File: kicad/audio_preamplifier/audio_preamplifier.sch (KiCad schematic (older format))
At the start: 33 parts, among them P1 CONN_01X05, P2 CONN_01X03, P3 CONN_01X03, P4 CONN_01X02, U1 PIC12F629, U2 78L05, U3 TL072

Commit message: new kicad version components in schematics
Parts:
- removed C10, C2, C3: 100n, symbol C
- removed P1: CONN_01X05, symbol CONN_01X05
- removed R1: 10k, symbol R
- removed R5, R6, R7: 3k3, symbol R
- removed U1: PIC12F629, SOIC, symbol PIC12F629
- removed U2: 78L05, symbol 78L05
- C1: value 100m -> 100m/25V; footprint (none) -> Capacitors_SMD:c_elec_6.3x7.7; symbol C -> CP
- C11: footprint (none) -> Capacitors_SMD:C_1206_HandSoldering
- C4: value 47m -> 47m/25V; footprint (none) -> Capacitors_Tantalum_SMD:TantalC_SizeD_EIA-7343_HandSoldering; symbol C -> CP
- C5: value 2m2 -> 2m2/16V; footprint (none) -> Capacitors_Tantalum_SMD:TantalC_SizeA_EIA-3216_HandSoldering; symbol C -> CP
- C6, C7: value 10m -> 10m/16V; footprint (none) -> Capacitors_SMD:c_elec_5x5.8; symbol C -> CP
- C8, C9: value 47m -> 47m/25V; footprint (none) -> Capacitors_SMD:c_elec_5x5.8; symbol C -> CP
- P2, P3: footprint (none) -> Pin_Headers:Pin_Header_Straight_1x03
- P4: footprint (none) -> Pin_Headers:Pin_Header_Straight_1x02
- R10, R11, R12, R13, R14, R15, R16, R17, R8, R9: footprint (none) -> Resistors_SMD:R_1206_HandSoldering
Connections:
- net labels added: 12V_filtered, virtual_gnd
- net labels removed: +5V, CLK, DataIn, DataOut, GND, POWER_CTL
- wire segments 84 -> 62
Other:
- moved on the sheet: C11, L1, P2, P3, P4, R10, R11, R12, R13, R14, R15, R16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

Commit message: update parts for new version of kicad
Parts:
- U3: symbol TL072 -> TL072-RESCUE-audio_preamplifier
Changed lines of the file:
@@
 EESchema Schematic File Version 2
+LIBS:audio_preamplifier-rescue
 LIBS:power
 LIBS:device
@@
 LIBS:contrib
 LIBS:valves
-LIBS:audio_preamplifier-rescue
 LIBS:audio_preamplifier-cache
 EELAYER 25 0
@@
 $EndComp
 $Comp
-L TL072 U3
+L TL072-RESCUE-audio_preamplifier U3
 U 2 1 52D3B907
 P 3850 3800
@@
 $EndComp
 $Comp
-L TL072 U3
+L TL072-RESCUE-audio_preamplifier U3
 U 1 1 52D3B8FE
 P 3900 1850

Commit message: fix values
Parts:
- removed P4: CONN_01X02, Pin_Headers:Pin_Header_Straight_1x02, symbol CONN_01X02
- P3: footprint Pin_Headers:Pin_Header_Straight_1x03 -> Pin_Headers:Pin_Header_Straight_1x05; symbol CONN_01X03 -> CONN_01X05
- R14, R15: value 330k -> 100k
- R16, R17: value 7M5 -> 2M2
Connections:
- net +12V: now also P3.5 (P5)
- net AGND: now also P3.4 (P4)
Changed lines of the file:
@@
 L AGND #PWR03
 U 1 1 52EA31C6
-P 7950 4900
-F 0 "#PWR03" H 7950 4900 40  0001 C CNN
-F 1 "AGND" H 7950 4830 50  0000 C CNN
-F 2 "" H 7950 4900 60  0001 C CNN
-F 3 "" H 7950 4900 60  0001 C CNN
-	1    7950 4900
+P 8100 4000
+F 0 "#PWR03" H 8100 4000 40  0001 C CNN
+F 1 "AGND" H 8100 3930 50  0000 C CNN
+F 2 "" H 8100 4000 60  0001 C CNN
+F 3 "" H 8100 4000 60  0001 C CNN
+	1    8100 4000
 	1    0    0    -1
 $EndComp
@@
 $EndComp
 $Comp
-L AGND #PWR010
+L AGND #PWR09
 U 1 1 52E56AD2
 P 7500 3500
-F 0 "#PWR010" H 7500 3500 40  0001 C CNN
+F 0 "#PWR09" H 7500 3500 40  0001 C CNN
 F 1 "AGND" H 7500 3430 50  0000 C CNN
 F 2 "" H 7500 3500 60  0001 C CNN
@@
 $EndComp
 $Comp
-L AGND #PWR011
+L AGND #PWR010
 U 1 1 52E56ACB
 P 7400 2400
-F 0 "#PWR011" H 7400 2400 40  0001 C CNN
+F 0 "#PWR010" H 7400 2400 40  0001 C CNN
 F 1 "AGND" H 7400 2330 50  0000 C CNN
 F 2 "" H 7400 2400 60  0001 C CNN
@@
 $EndComp
 $Comp
-L +12V #PWR012
+L +12V #PWR011
 U 1 1 52D3D406
-P 7950 4450
-F 0 "#PWR012" H 7950 4400 20  0001 C CNN
-F 1 "+12V" H 7950 4550 30  0000 C CNN
-F 2 "" H 7950 4450 60  0001 C CNN
-F 3 "" H 7950 4450 60  0001 C CNN
-	1    7950 4450
+P 7250 3550
+F 0 "#PWR011" H 7250 3500 20  0001 C CNN
+F 1 "+12V" H 7250 3650 30  0000 C CNN
+F 2 "" H 7250 3550 60  0001 C CNN
+F 3 "" H 7250 3550 60  0001 C CNN
+	1    7250 3550
 	1    0    0    -1
 $EndComp
@@
 right_out
 $Comp
-L +12V #PWR014
+L +12V #PWR012
 U 1 1 52D3D226
 P 2700 5800
-F 0 "#PWR014" H 2700 5750 20  0001 C CNN
+F 0 "#PWR012" H 2700 5750 20  0001 C CNN
 F 1 "+12V" H 2700 5900 30  0000 C CNN
 F 2 "" H 2700 5800 60  0001 C CNN
@@
 P 3350 4850
 F 0 "R15" V 3430 4850 50  0000 C CNN
-F 1 "330k" V 3350 4850 50  0000 C CNN
+F 1 "100k" V 3350 4850 50  0000 C CNN
 F 2 "Resistors_SMD:R_1206_HandSoldering" H 3350 4850 60  0001 C CNN
 F 3 "" H 3350 4850 60  0001 C CNN
@@
 P 3400 2700
 F 0 "R14" V 3480 2700 50  0000 C CNN
-F 1 "330k" V 3400 2700 50  0000 C CNN
+F 1 "100k" V 3400 2700 50  0000 C CNN
 F 2 "Resistors_SMD:R_1206_HandSoldering" H 3400 2700 60  0001 C CNN
 F 3 "" H 3400 2700 60  0001 C CNN
@@
 P 4250 4400
 F 0 "R17" V 4330 4400 50  0000 C CNN
-F 1 "7M5" V 4250 4400 50  0000 C CNN
+F 1 "2M2" V 4250 4400 50  0000 C CNN
 F 2 "Resistors_SMD:R_1206_HandSoldering" H 4250 4400 60  0001 C CNN
 F 3 "" H 4250 4400 60  0001 C CNN
@@
 P 4150 2350
 F 0 "R16" V 4230 2350 50  0000 C CNN
-F 1 "7M5" V 4150 2350 50  0000 C CNN
+F 1 "2M2" V 4150 2350 50  0000 C CNN
 F 2 "Resistors_SMD:R_1206_HandSoldering" H 4150 2350 60  0001 C CNN
 F 3 "" H 4150 2350 60  0001 C CNN
@@
 $EndComp
 $Comp
-L CONN_01X02 P4
-U 1 1 54F9CC01
-P 8400 4600
-F 0 "P4" H 8400 4750 50  0000 C CNN
-F 1 "CONN_01X02" V 8500 4600 50  0000 C CNN
-F 2 "Pin_Headers:Pin_Header_Straight_1x02" H 8400 4600 60  0000 C CNN
-F 3 "" H 8400 4600 60  0000 C CNN
-	1    8400 4600
-	1    0    0    -1
-$EndComp
-$Comp
-L CONN_01X03 P3
+L CONN_01X05 P3
 U 1 1 54F9D72B
-P 8400 3450
-F 0 "P3" H 8400 3650 50  0000 C CNN
-F 1 "CONN_01X03" V 8500 3450 50  0000 C CNN
-F 2 "Pin_Headers:Pin_Header_Straight_1x03" H 8400 3450 60  0000 C CNN
-F 3 "" H 8400 3450 60  0000 C CNN
-	1    8400 3450
+P 8400 3550
+F 0 "P3" H 8400 3750 50  0000 C CNN
+F 1 "CONN_01X03" V 8500 3550 50  0000 C CNN
+F 2 "Pin_Headers:Pin_Header_Straight_1x05" H 8400 3550 60  0000 C CNN
+F 3 "" H 8400 3550 60  0000 C CNN
+	1    8400 3550
 	1    0    0    -1
 $EndComp
@@
 $EndComp
 $Comp
-L AGND #PWR020
+L AGND #PWR013
 U 1 1 560EBEB5
 P 4150 6700
-F 0 "#PWR020" H 4150 6700 40  0001 C CNN
+F 0 "#PWR013" H 4150 6700 40  0001 C CNN
 F 1 "AGND" H 4150 6630 50  0000 C CNN
 F 2 "" H 4150 6700 60  0001 C CNN
@@
 12V_filtered
 Wire Wire Line
-	7950 4650 7950 4900
+	8100 3650 8100 4000
 Wire Wire Line
 	3800 2550 3800 2250
 Wire Wire Line
-	7950 4450 7950 4550
+	7250 3550 7250 3750
 Wire Wire Line
 	2700 6400 2700 6650
@@
 Wire Wire Line
 	2700 5800 2700 6100
-Wire Wire Line
-	7950 4550 8200 4550
-Wire Wire Line
-	8200 4650 7950 4650
 Wire Wire Line
 	3450 5900 4950 5900
@@
 Wire Wire Line
 	2700 1750 3400 1750
+Wire Wire Line
+	8100 3650 8200 3650
+Wire Wire Line
+	7250 3750 8200 3750
 $EndSCHEMATC

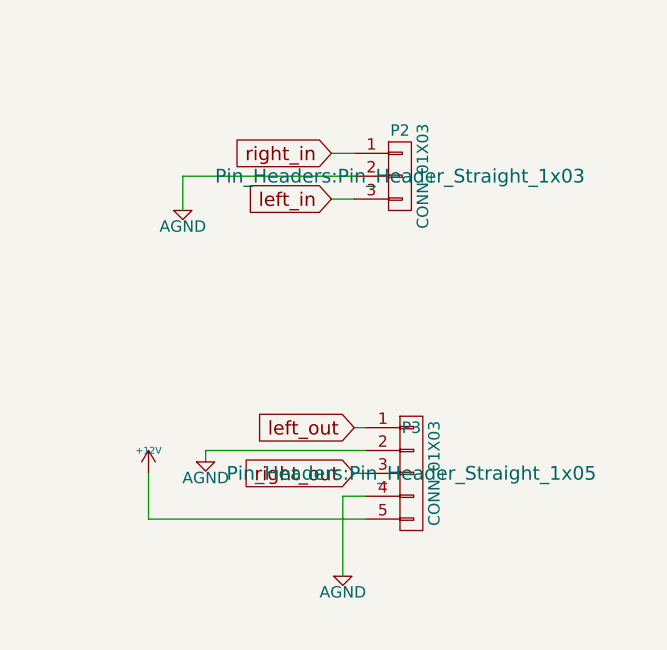
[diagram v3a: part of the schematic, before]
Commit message: assamble plan, BOM
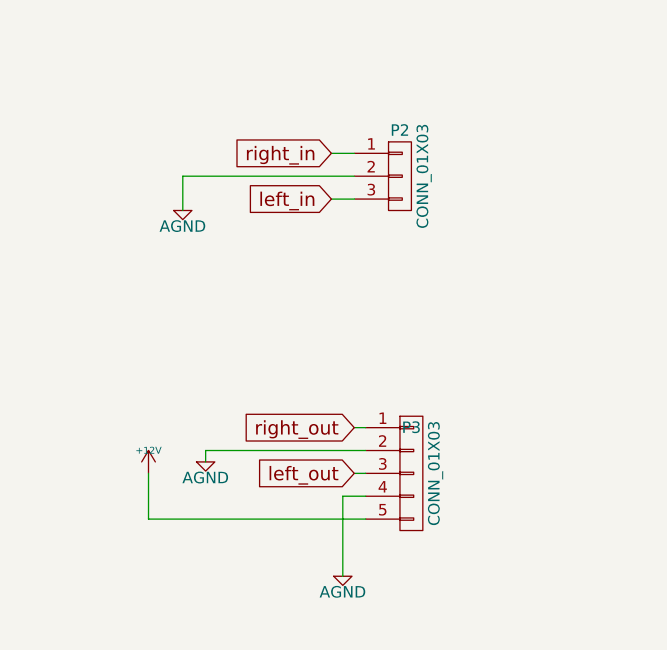
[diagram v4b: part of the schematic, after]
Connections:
- net left_out: now also P3.3 (P3); no longer P3.1 (P1)
- net right_out: now also P3.1 (P1); no longer P3.3 (P3)
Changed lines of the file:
@@
 Text GLabel 8050 2150 0    60   Input ~ 0
 right_in
+Text GLabel 8150 3550 0    60   Input ~ 0
+left_out
 Text GLabel 8150 3350 0    60   Input ~ 0
-left_out
-Text GLabel 8150 3550 0    60   Input ~ 0
 right_out
 $Comp
@@
 F 0 "P3" H 8400 3750 50  0000 C CNN
 F 1 "CONN_01X03" V 8500 3550 50  0000 C CNN
-F 2 "Pin_Headers:Pin_Header_Straight_1x05" H 8400 3550 60  0000 C CNN
+F 2 "Pin_Headers:Pin_Header_Straight_1x05" H 8400 3550 60  0001 C CNN
 F 3 "" H 8400 3550 60  0000 C CNN
 	1    8400 3550
@@
 F 0 "P2" H 8350 2450 50  0000 C CNN
 F 1 "CONN_01X03" V 8450 2250 50  0000 C CNN
-F 2 "Pin_Headers:Pin_Header_Straight_1x03" H 8350 2250 60  0000 C CNN
+F 2 "Pin_Headers:Pin_Header_Straight_1x03" H 8350 2250 60  0001 C CNN
 F 3 "" H 8350 2250 60  0000 C CNN
 	1    8350 2250
